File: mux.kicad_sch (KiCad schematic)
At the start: 30 parts, among them U711 TMUX7219, U712 TMUX7219, U713 TMUX7219, U714 TMUX7219, U715 TMUX7219, U716 TMUX7219, U717 74HC595

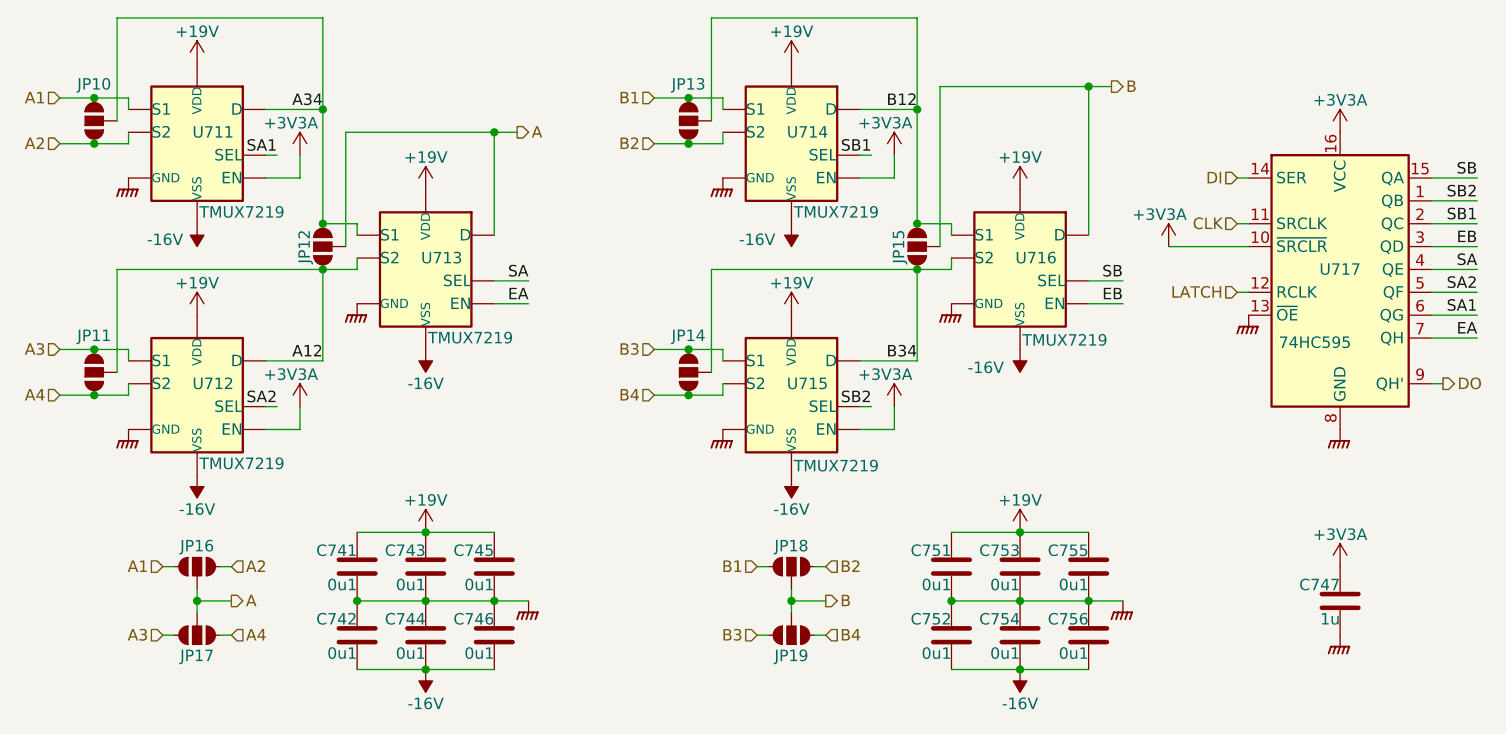
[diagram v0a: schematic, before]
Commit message: Remove silly jumpers.
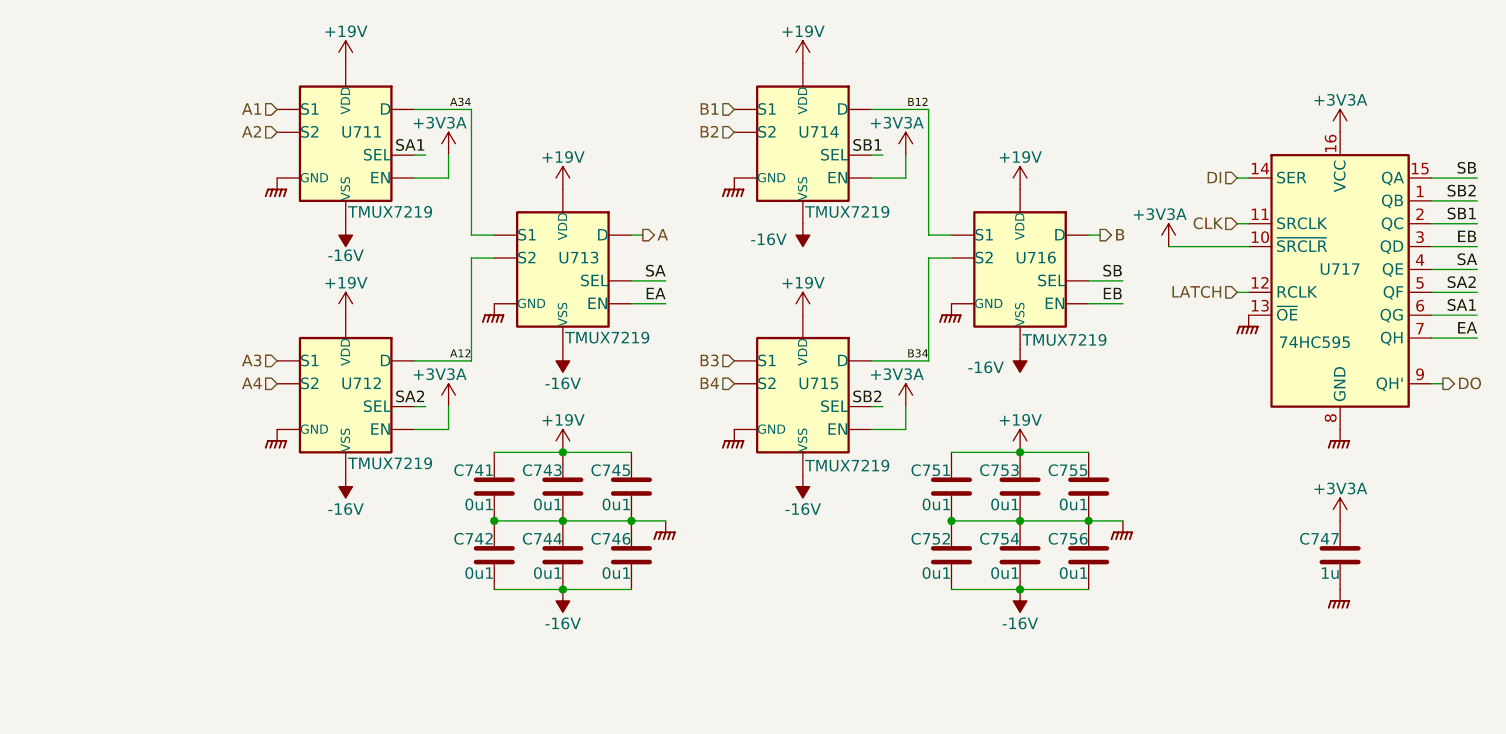
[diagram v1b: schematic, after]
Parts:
- removed JP10, JP11, JP12, JP13, JP14, JP15, JP16, JP17, JP18, JP19: SolderJumper_3_Open, Parts:Jumper3Open, symbol Parts:SolderJumper_3_Open
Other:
- moved on the sheet: C741, C742, C743, C744, C745, C746, C747, C751, C752, C753, C754, C755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

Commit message: More component metadata.
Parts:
- C741, C742, C743, C744, C745, C746, C747, C751, C752, C753, C754, C755, C756, U717: Stock (none) -> JLC
- U711, U712, U713, U714, U715, U716: LCSC (none) -> C2862901; Stock (none) -> JLC
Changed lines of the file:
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@@
 			)
 		)
-		(property "Stock" ""
+		(property "Stock" "JLC"
 			(at 170.18 106.68 0)
 			(effects
@@
 			)
 		)
-		(property "Stock" ""
+		(property "Stock" "JLC"
 			(at 170.18 99.06 0)
 			(effects
@@
 			)
 		)
+		(property "LCSC" "C2862901"
+			(at 146.05 60.96 0)
+			(effects
+				(font
+					(size 1.27 1.27)
+				)
+				(hide yes)
+			)
+		)
+		(property "Stock" "JLC"
+			(at 146.05 60.96 0)
+			(effects
+				(font
+					(size 1.27 1.27)
+				)
+				(hide yes)
+			)
+		)
 		(pin "3"
 		)
@@
 			)
 		)
+		(property "LCSC" "C2862901"
+			(at 146.05 88.9 0)
+			(effects
+				(font
+					(size 1.27 1.27)
+				)
+				(hide yes)
+			)
+		)
+		(property "Stock" "JLC"
+			(at 146.05 88.9 0)
+			(effects
+				(font
+					(size 1.27 1.27)
+				)
+				(hide yes)
+			)
+		)
 		(pin "3"
 		)
@@
 			)
 		)
-		(property "Stock" ""
+		(property "Stock" "JLC"
 			(at 111.76 99.06 0)
 			(effects
@@
 			)
 		)
-		(property "Stock" ""
+		(property "Stock" "JLC"
 			(at 111.76 106.68 0)
 			(effects
@@
 			)
 		)
+		(property "LCSC" "C2862901"
+			(at 119.38 74.93 0)
+			(effects
+				(font
+					(size 1.27 1.27)
+				)
+				(hide yes)
+			)
+		)
+		(property "Stock" "JLC"
+			(at 119.38 74.93 0)
+			(effects
+				(font
+					(size 1.27 1.27)
+				)
+				(hide yes)
+			)
+		)
 		(pin "3"
 		)
@@
 			)
 		)
-		(property "Stock" ""
+		(property "Stock" "JLC"
 			(at 205.74 74.93 0)
 			(effects
@@
 			)
 		)
-		(property "Stock" ""
+		(property "Stock" "JLC"
 			(at 162.56 99.06 0)
 			(effects
@@
 			)
 		)
-		(property "Stock" ""
+		(property "Stock" "JLC"
 			(at 127 99.06 0)
 			(effects
@@
 			)
 		)
+		(property "LCSC" "C2862901"
+			(at 95.25 88.9 0)
+			(effects
+				(font
+					(size 1.27 1.27)
+				)
+				(hide yes)
+			)
+		)
+		(property "Stock" "JLC"
+			(at 95.25 88.9 0)
+			(effects
+				(font
+					(size 1.27 1.27)
+				)
+				(hide yes)
+			)
+		)
 		(pin "3"
 		)
@@
 			)
 		)
-		(property "Stock" ""
+		(property "Stock" "JLC"
 			(at 119.38 106.68 0)
 			(effects
@@
 			)
 		)
-		(property "Stock" ""
+		(property "Stock" "JLC"
 			(at 205.74 106.68 0)
 			(effects
@@
 			)
 		)
-		(property "Stock" ""
+		(property "Stock" "JLC"
 			(at 119.38 99.06 0)
 			(effects
@@
 			)
 		)
-		(property "Stock" ""
+		(property "Stock" "JLC"
 			(at 162.56 106.68 0)
 			(effects
@@
 			)
 		)
+		(property "LCSC" "C2862901"
+			(at 95.25 60.96 0)
+			(effects
+				(font
+					(size 1.27 1.27)
+				)
+				(hide yes)
+			)
+		)
+		(property "Stock" "JLC"
+			(at 95.25 60.96 0)
+			(effects
+				(font
+					(size 1.27 1.27)
+				)
+				(hide yes)
+			)
+		)
 		(pin "3"
 		)
@@
 			)
 		)
-		(property "Stock" ""
+		(property "Stock" "JLC"
 			(at 177.8 99.06 0)
 			(effects
@@
 			)
 		)
-		(property "Stock" ""
+		(property "Stock" "JLC"
 			(at 177.8 106.68 0)
 			(effects
@@
 			)
 		)
+		(property "LCSC" "C2862901"
+			(at 170.18 74.93 0)
+			(effects
+				(font
+					(size 1.27 1.27)
+				)
+				(hide yes)
+			)
+		)
+		(property "Stock" "JLC"
+			(at 170.18 74.93 0)
+			(effects
+				(font
+					(size 1.27 1.27)
+				)
+				(hide yes)
+			)
+		)
 		(pin "3"
 		)
@@
 			)
 		)
-		(property "Stock" ""
+		(property "Stock" "JLC"
 			(at 127 106.68 0)
 			(effects
